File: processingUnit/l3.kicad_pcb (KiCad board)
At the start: 2 copper layers, 168.8 x 115 mm, 13 parts, among them J1 Conn_01x04, J2 Conn_01x06, J3 Conn_01x06, J4 Conn_01x06, J5 Conn_01x06, SW1 SW_SPDT, SW2 SW_SPDT, SW5 SW_SPDT, U2 BNO085, U3 >VALUE

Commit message: rough ideation
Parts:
- removed J1: Conn_01x04, Connector_JST:JST_XH_S4B-XH-A_1x04_P2.50mm_Horizontal
- removed J2, J3, J4, J5: Conn_01x06, Connector_JST:JST_SH_BM06B-SRSS-TB_1x06-1MP_P1.00mm_Vertical
- removed R1, R2: 1K, l3:res0603
- removed SW1, SW2, SW5: SW_SPDT, l3:SS12D00G3
- removed U1: ~, l3:OpenMV_RT
- removed U2: BNO085, l3:bno085
- removed U3: >VALUE, l3:xiao-esp32c3
- added C101: 2u2, Library:cap0603, F.Cu at (-13.5, 70.9)
- added C102: 2u2, Library:cap0603, F.Cu at (-13.5, 74.0)
- added C103: 2u2, Library:cap0603, F.Cu at (-13.5, 77.1)
- added C104: 2u2, Library:cap0603, F.Cu at (-13.5, 80.2)
- added C201: 100u, Capacitor_THT:CP_Radial_D8.0mm_P3.50mm, F.Cu at (-62.1, 74.1)
- added C202: 100u, Capacitor_THT:CP_Radial_D8.0mm_P3.50mm, F.Cu at (-62.1, 83.7)
- added C203: 0u1, Library:cap0603, F.Cu at (-43.7, 84.5)
- added C204: 0u1, Library:cap0603, F.Cu at (-43.7, 87.5)
- added C205: 100u, Capacitor_THT:CP_Radial_D8.0mm_P3.50mm, F.Cu at (-62.1, 93.2)
- added C206: 100u, Capacitor_THT:CP_Radial_D8.0mm_P3.50mm, F.Cu at (-62.1, 102.8)
- added C207: 0u1, Library:cap0603, F.Cu at (-43.7, 90.7)
- added C208: 0u1, Library:cap0603, F.Cu at (-43.7, 93.8)
- added C326: 2u2, Library:cap0603, F.Cu at (-63.0, 127.7)
- added C327: 0u1, Library:cap0603, F.Cu at (-63.0, 130.8)
- added C328: 0u1, Library:cap0603, F.Cu at (-63.0, 133.9)
- added C329: 0u1, Library:cap0603, F.Cu at (-63.0, 137.0)
- added C330: 0u1, Library:cap0603, F.Cu at (-58.3, 127.7)
- added C331: 0u1, Library:cap0603, F.Cu at (-58.3, 130.8)
- added C332: 0u1, Library:cap0603, F.Cu at (-58.3, 133.9)
- added C333: 2u2, Library:cap0603, F.Cu at (-58.3, 137.0)
- added C334: 0u1, Library:cap0603, F.Cu at (-53.6, 127.7)
- added C335: 10p, Library:cap0603, F.Cu at (-53.6, 130.8)
- added C336: 10p, Library:cap0603, F.Cu at (-53.6, 133.9)
- added C337: 10p, Library:cap0603, F.Cu at (-53.6, 137.0)
- added C338: 10p, Library:cap0603, F.Cu at (-48.9, 127.7)
- added C401: 2u2, Library:cap0603, F.Cu at (-34.8, 113.2)
- added C402: 0u1, Library:cap0603, F.Cu at (-34.8, 116.3)
- added C403: 0u1, Library:cap0603, F.Cu at (-34.8, 119.5)
- added C404: 0u1, Library:cap0603, F.Cu at (-34.8, 122.5)
- added C405: 0u1, Library:cap0603, F.Cu at (-34.8, 125.7)
- added C406: 0u1, Library:cap0603, F.Cu at (-34.8, 128.8)
- added C407: 0u1, Library:cap0603, F.Cu at (-34.8, 131.8)
- added C408: 10p, Library:cap0603, F.Cu at (-30.1, 113.2)
- added C409: 10p, Library:cap0603, F.Cu at (-30.1, 116.3)
- added C410: 0u1, Library:cap0603, F.Cu at (31.8, 138.8)
- added C411: 2u2, Library:cap0603, F.Cu at (31.8, 136.6)
- added C412: 10n, Library:cap0603, F.Cu at (34.7, 134.0)
- added C413: 0u1, Library:cap0603, F.Cu at (36.9, 134.0)
- added D304: RCLAMP0521PATCT, Library:RCLAMP0521PATCT, F.Cu at (-49.1, 120.0)
- added D305: RCLAMP0521PATCT, Library:RCLAMP0521PATCT, F.Cu at (-49.1, 122.8)
- added D306: RED, Library:led0603, F.Cu at (-48.9, 130.8)
- added D401: RCLAMP0521PATCT, Library:RCLAMP0521PATCT, F.Cu at (-14.2, 113.0)
- added D402: RCLAMP0521PATCT, Library:RCLAMP0521PATCT, F.Cu at (-14.2, 115.8)
- added D403: RED, Library:led0603, F.Cu at (43.6, 150.8)
- added FB101: 100R, Library:fb0603, F.Cu at (-13.5, 83.3)
- added FB102: 100R, Library:fb0603, F.Cu at (-13.5, 86.4)
- added IC201: TB67H450FNG,EL, Library:P-HSOP8-0405-1p27-001_TOS, F.Cu at (-50.6, 86.2)
- added IC202: TB67H450FNG,EL, Library:P-HSOP8-0405-1p27-001_TOS, F.Cu at (-50.6, 93.0)
- added IC203: TB67H450FNG,EL, Library:P-HSOP8-0405-1p27-001_TOS, F.Cu at (-50.6, 99.7)
- added IC204: TB67H450FNG,EL, Library:P-HSOP8-0405-1p27-001_TOS, F.Cu at (-50.6, 106.3)
- added IC401: ICM-42688-P, Library:IIM42352, F.Cu at (35.8, 137.7)
- added J101: +12V, Library:xt30-f, F.Cu at (101.4, 95.6)
- added J102: Conn_01x05, Connector_JST:JST_XH_B5B-XH-A_1x05_P2.50mm_Vertical, F.Cu at (108.4, 90.4)
- added J103: Conn_01x04, Connector_JST:JST_XH_B4B-XH-A_1x04_P2.50mm_Vertical, F.Cu at (181.0, 111.3)
- added J104: Conn_01x04, Connector_JST:JST_XH_B4B-XH-A_1x04_P2.50mm_Vertical, B.Cu at (187.8, 111.3)
- added J201: FL, Connector_JST:JST_XH_S2B-XH-A_1x02_P2.50mm_Horizontal, F.Cu at (-52.1, 72.7)
- added J202: FR, Connector_JST:JST_XH_S2B-XH-A_1x02_P2.50mm_Horizontal, F.Cu at (-42.7, 72.7)
- added J203: BL, Connector_JST:JST_XH_S2B-XH-A_1x02_P2.50mm_Horizontal, F.Cu at (-33.2, 72.7)
- added J204: BR, Connector_JST:JST_XH_S2B-XH-A_1x02_P2.50mm_Horizontal, F.Cu at (-23.8, 72.7)
- added J309: Conn_01x04, Connector_JST:JST_XH_B4B-XH-A_1x04_P2.50mm_Vertical, F.Cu at (187.8, 97.8)
- added J401: Conn_01x04, Connector_JST:JST_XH_B4B-XH-A_1x04_P2.50mm_Vertical, F.Cu at (181.0, 97.8)
- added Q401: NTR1P02T1G, Package_TO_SOT_SMD:SOT-23, F.Cu at (203.8, 100.2)
- added R201: 10K, Library:res0603, F.Cu at (-39.0, 84.5)
- added R202: 10K, Library:res0603, F.Cu at (-39.0, 87.5)
- added R203: 20, Library:res0603, F.Cu at (-39.0, 90.7)
- added R204: 20, Library:res0603, F.Cu at (-39.0, 93.8)
- added R205: 10K, Library:res0603, F.Cu at (-34.3, 84.5)
- added R206: 10K, Library:res0603, F.Cu at (-34.3, 87.5)
- added R207: 20, Library:res0603, F.Cu at (-34.3, 90.7)
- added R208: 20, Library:res0603, F.Cu at (-34.3, 93.8)
- added R313: 10K, Library:res0603, F.Cu at (-48.9, 133.9)
- added R314: 1K, Library:res0603, F.Cu at (-48.9, 137.0)
- added R401: R, Library:res0603, F.Cu at (-25.4, 113.2)
- added R402: R, Library:res0603, F.Cu at (40.4, 136.5)
- added R403: R, Library:res0603, F.Cu at (40.4, 139.6)
- added R404: 1K, Library:res0603, F.Cu at (43.7, 148.6)
- added R405: 10K, Library:res0603, F.Cu at (203.7, 104.0)
- added SW303: SW_Push, Library:SW_PUSH_SPST, F.Cu at (-43.9, 120.9)
- added SW401: SW_Push, Library:SW_PUSH_SPST, F.Cu at (-19.5, 113.9)
- added SW402: SW_Push, Library:SW_PUSH_SPST, F.Cu at (193.6, 100.8)
- added U303: STM32F446RET, Package_QFP:LQFP-64_10x10mm_P0.5mm, F.Cu at (-58.1, 118.9)
- added U304: 16MHz, Library:830108288709, F.Cu at (-44.2, 135.5)
- added U401: STM32F103CBTX, Package_QFP:LQFP-48_7x7mm_P0.5mm, F.Cu at (36.0, 146.7)
- added U402: 16MHz, Library:830108288709, F.Cu at (-20.7, 129.9)
- added Y301: 32.768 kHz, Library:830003000, F.Cu at (-45.0, 115.2)
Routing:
- removed copper zone on B.Cu, net GND
- removed copper zone on F.Cu, net GND
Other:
- board outline removed

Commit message: yes
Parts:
- removed C326, C333, C401, C411: 2u2, Library:cap0603
- removed C327, C328, C329, C330, C331, C332, C334, C402, C403, C404, C405, C406, C407, C410, C413: 0u1, Library:cap0603
- removed C335, C336, C337, C338, C408, C409: 10p, Library:cap0603
- removed C412: 10n, Library:cap0603
- removed D304, D305, D401, D402: RCLAMP0521PATCT, Library:RCLAMP0521PATCT
- removed D306, D403: RED, Library:led0603
- removed IC202, IC203, IC204: TB67H450FNG,EL, Library:P-HSOP8-0405-1p27-001_TOS
- removed IC401: ICM-42688-P, Library:IIM42352
- removed J202: FR, Connector_JST:JST_XH_S2B-XH-A_1x02_P2.50mm_Horizontal
- removed J203: BL, Connector_JST:JST_XH_S2B-XH-A_1x02_P2.50mm_Horizontal
- removed J204: BR, Connector_JST:JST_XH_S2B-XH-A_1x02_P2.50mm_Horizontal
- removed J309, J401: Conn_01x04, Connector_JST:JST_XH_B4B-XH-A_1x04_P2.50mm_Vertical
- removed Q401: NTR1P02T1G, Package_TO_SOT_SMD:SOT-23
- removed R206, R313, R405: 10K, Library:res0603
- removed R207, R208: 20, Library:res0603
- removed R314, R404: 1K, Library:res0603
- removed R401, R402, R403: R, Library:res0603
- removed SW303, SW401, SW402: SW_Push, Library:SW_PUSH_SPST
- removed U303: STM32F446RET, Package_QFP:LQFP-64_10x10mm_P0.5mm
- removed U304, U402: 16MHz, Library:830108288709
- removed U401: STM32F103CBTX, Package_QFP:LQFP-48_7x7mm_P0.5mm
- added C209: 10n, Library:cap0603, F.Cu at (39.7, 82.5)
- added C210: 0u1, Library:cap0603, F.Cu at (39.7, 85.6)
- added C211: 0u1, Library:cap0603, F.Cu at (39.7, 88.7)
- added C212: 10p, Library:cap0603, F.Cu at (39.7, 91.8)
- added C213: 10p, Library:cap0603, F.Cu at (39.7, 94.9)
- added C301: 0u1, Library:cap0603, F.Cu at (35.0, 42.4)
- added C302: 10p, Library:cap0603, F.Cu at (35.0, 45.5)
- added C303: 10p, Library:cap0603, F.Cu at (35.0, 48.6)
- added C304: 10p, Library:cap0603, F.Cu at (35.0, 51.7)
- added C305: 10p, Library:cap0603, F.Cu at (39.7, 42.4)
- added C306: 2u2, Library:cap0603, F.Cu at (39.7, 45.5)
- added C307: 2u2, Library:cap0603, F.Cu at (39.7, 48.6)
- added C308: 0u1, Library:cap0603, F.Cu at (39.7, 51.7)
- added C309: 0u1, Library:cap0603, F.Cu at (44.4, 42.4)
- added C310: 0u1, Library:cap0603, F.Cu at (44.4, 45.5)
- added C311: 0u1, Library:cap0603, F.Cu at (44.4, 48.6)
- added C312: 0u1, Library:cap0603, F.Cu at (44.4, 51.7)
- added C313: 0u1, Library:cap0603, F.Cu at (49.1, 42.4)
- added D201: RCLAMP0521PATCT, Library:RCLAMP0521PATCT, F.Cu at (55.6, 94.8)
- added D202: RCLAMP0521PATCT, Library:RCLAMP0521PATCT, F.Cu at (55.6, 97.5)
- added D203: RED, Library:led0603, F.Cu at (39.7, 98.0)
- added D301: RED, Library:led0603, F.Cu at (49.1, 45.5)
- added D302: RCLAMP0521PATCT, Library:RCLAMP0521PATCT, F.Cu at (53.2, 46.7)
- added D303: RCLAMP0521PATCT, Library:RCLAMP0521PATCT, F.Cu at (53.2, 49.4)
- added J301: Conn_01x04, Connector_JST:JST_XH_B4B-XH-A_1x04_P2.50mm_Vertical, F.Cu at (36.1, 56.6)
- added Q201: NTR1P02T1G, Package_TO_SOT_SMD:SOT-23, F.Cu at (49.6, 72.5)
- added R301: 1K, Library:res0603, F.Cu at (49.1, 48.6)
- added R302: 10K, Library:res0603, F.Cu at (49.1, 51.7)
- added SW201: SW_Push, Library:SW_PUSH_SPST, F.Cu at (50.3, 91.5)
- added SW202: SW_Push, Library:SW_PUSH_SPST, F.Cu at (50.3, 95.9)
- added SW301: SW_Push, Library:SW_PUSH_SPST, F.Cu at (55.0, 43.1)
- added U201: STM32F103CBTX, Package_QFP:LQFP-48_7x7mm_P0.5mm, F.Cu at (52.5, 83.5)
- added U202: 16MHz, Library:830108288709, F.Cu at (56.1, 91.3)
- added U301: STM32F446RET, Package_QFP:LQFP-64_10x10mm_P0.5mm, F.Cu at (54.4, 60.5)
- added U302: 16MHz, Library:830108288709, F.Cu at (57.3, 47.5)
- C201: value 100u -> 2u2; footprint Capacitor_THT:CP_Radial_D8.0mm_P3.50mm -> Library:cap0603
- C202, C205, C206: value 100u -> 0u1; footprint Capacitor_THT:CP_Radial_D8.0mm_P3.50mm -> Library:cap0603
- C208: value 0u1 -> 2u2
- IC201: value TB67H450FNG,EL -> ICM-42688-P; footprint Library:P-HSOP8-0405-1p27-001_TOS -> Library:IIM42352
- J104: moved to F.Cu
- J201: value FL -> Conn_01x04; footprint Connector_JST:JST_XH_S2B-XH-A_1x02_P2.50mm_Horizontal -> Connector_JST:JST_XH_B4B-XH-A_1x04_P2.50mm_Vertical
- R202: value 10K -> R
- R203, R204: value 20 -> R
- R205: value 10K -> 1K
- moved J104 125.8 mm to (64.0, 89.0), turned to 0 degrees
- moved J103 120.8 mm to (64.0, 81.2), turned to 0 degrees
- moved IC201 105.9 mm to (54.4, 72.2)
- moved Y301 97.7 mm to (38.6, 64.6)
- moved C206 97.5 mm to (35.0, 94.9)
- moved C201 97.3 mm to (35.0, 79.4)
- moved C205 97.2 mm to (35.0, 91.8)
- moved C202 97.2 mm to (35.0, 82.5)
- moved C101 91.1 mm to (77.3, 79.4)
- moved C102 91.1 mm to (77.3, 82.5)
- moved C103 91.1 mm to (77.3, 85.6)
- moved C104 91.1 mm to (77.3, 88.7)
- moved FB101 91.1 mm to (77.3, 91.8)
- moved FB102 91.1 mm to (77.3, 94.9)
- moved J201 88.3 mm to (36.1, 73.5)
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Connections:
- C201 pad 1: +12V -> +3V3 FILT
- C202 pad 1: +12V -> +3V3 FILT
- C203 pad 1: /Motor Driver/FL VREF -> +3V3 FILT
- C204 pad 1: /Motor Driver/FR VREF -> +3V3 FILT
- C205 pad 1: +12V -> +3V3 FILT
- C206 pad 1: +12V -> +3V3 FILT
- C207 pad 1: /Motor Driver/BL VREF -> Net-(IC201-VDD)
- C208 pad 1: /Motor Driver/BR VREF -> Net-(IC201-VDD)
- IC201 pad 1: GNDREF -> unconnected-(IC201-SDO-Pad1)
- IC201 pad 2: FL IN 2 -> GNDREF
- IC201 pad 3: FL IN 1 -> GNDREF
- IC201 pad 4: /Motor Driver/FL VREF -> unconnected-(IC201-INT1-Pad4)
- IC201 pad 5: +12V -> Net-(IC201-VDD)
- IC201 pad 6: /Motor Driver/FL OUT 1 -> GNDREF
- IC201 pad 7: Net-(IC201-RS) -> GNDREF
- IC201 pad 8: /Motor Driver/FL OUT 2 -> Net-(IC201-VDD)
- IC201 pad 9: GNDREF -> unconnected-(IC201-INT2-Pad9)
- J201 pad 1: /Motor Driver/FL OUT 1 -> +3V3
- J201 pad 2: /Motor Driver/FL OUT 2 -> /IMU/MCU SWDIO
- R201 pad 1: +5V FILT -> Net-(Q201-G)
- R201 pad 2: /Motor Driver/FL VREF -> GNDREF
- R202 pad 1: +5V FILT -> GNDREF
- R202 pad 2: /Motor Driver/FR VREF -> /IMU/MCU BOOT0
- R203 pad 1: Net-(IC201-RS) -> +3V3 FILT
- R203 pad 2: GNDREF -> /IMU/MPU SDA
- R204 pad 1: Net-(IC202-RS) -> +3V3 FILT
- R204 pad 2: GNDREF -> /IMU/MPU SCL
- R205 pad 1: +5V FILT -> Net-(D203-K)
- R205 pad 2: /Motor Driver/BL VREF -> GNDREF

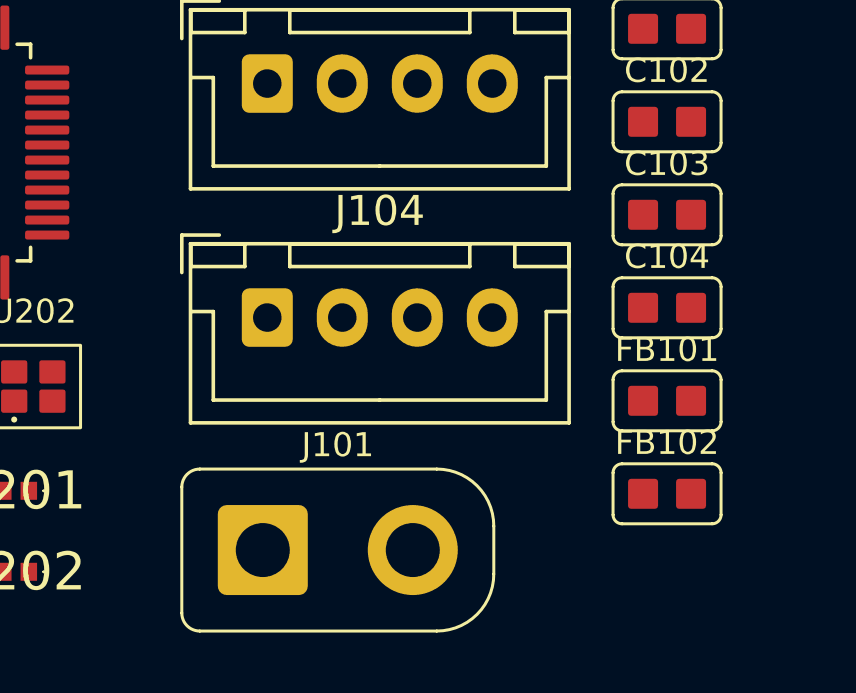
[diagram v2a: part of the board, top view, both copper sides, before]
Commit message: modified motor driver removed topInterface
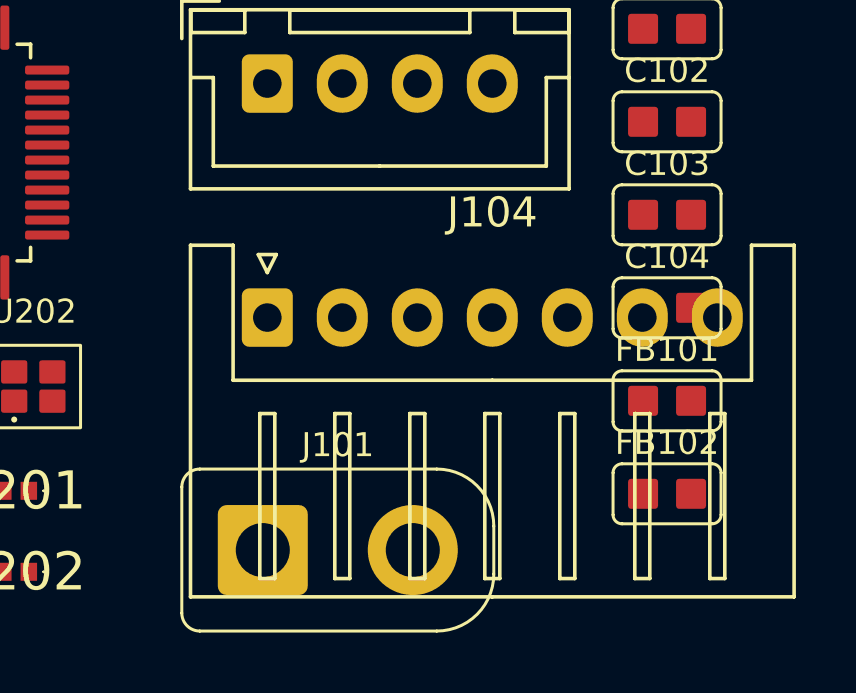
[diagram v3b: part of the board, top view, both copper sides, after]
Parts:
- J104: value Conn_01x04 -> Conn_01x07; footprint Connector_JST:JST_XH_B4B-XH-A_1x04_P2.50mm_Vertical -> Connector_JST:JST_XH_S7B-XH-A_1x07_P2.50mm_Horizontal
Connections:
- J104 pad 1: +5V -> +3V3
- J104 pad 4: GNDREF -> unconnected-(J104-Pin_4-Pad4)

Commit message: 死
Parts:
- removed C208: 2u2, Library:cap0603
- removed C209: 10n, Library:cap0603
- removed C210, C211, C311, C312, C313: 0u1, Library:cap0603
- removed C212, C213: 10p, Library:cap0603
- removed D202, D302, D303: RCLAMP0521PATCT, Library:RCLAMP0521PATCT
- removed D203: RED, Library:led0603
- removed IC201: ICM-42688-P, Library:IIM42352
- removed J104: Conn_01x07, Connector_JST:JST_XH_S7B-XH-A_1x07_P2.50mm_Horizontal
- removed J201, J301: Conn_01x04, Connector_JST:JST_XH_B4B-XH-A_1x04_P2.50mm_Vertical
- removed Q201: NTR1P02T1G, Package_TO_SOT_SMD:SOT-23
- removed R203, R204: R, Library:res0603
- removed R205: 1K, Library:res0603
- removed SW202: SW_Push, Library:SW_PUSH_SPST
- removed U202: 16MHz, Library:830108288709
- added R303: 4K7, Library:res0603, F.Cu at (61.5, 24.7)
- added R304: 4K7, Library:res0603, F.Cu at (61.5, 27.8)
- added R305: 1K, Library:res0603, F.Cu at (61.5, 30.9)
- added SW302: IMU RST, Button_Switch_THT:SW_PUSH_6mm, F.Cu at (47.0, 43.0)
- added Y201: 8Mhz, Crystal:Resonator_SMD_Murata_CSTxExxV-3Pin_3.0x1.1mm, F.Cu at (47.6, 68.8)
- C207, C309, C310: value 0u1 -> C
- C301: value 0u1 -> 2u2
- C302, C304, C305: value 10p -> 0u1
- C303: value 10p -> 2u2
- C306, C307: value 2u2 -> 0u1
- D201: value RCLAMP0521PATCT -> RED; footprint Library:RCLAMP0521PATCT -> Library:led0603
- J101: value +12V -> Conn_01x05; footprint Library:xt30-f -> Connector_JST:JST_XH_B5B-XH-A_1x05_P2.50mm_Vertical
- J102: value Conn_01x05 -> Conn_01x04; footprint Connector_JST:JST_XH_B5B-XH-A_1x05_P2.50mm_Vertical -> Connector_JST:JST_XH_B4B-XH-A_1x04_P2.50mm_Vertical
- J103: value Conn_01x04 -> Conn_01x07; footprint Connector_JST:JST_XH_B4B-XH-A_1x04_P2.50mm_Vertical -> Connector_JST:JST_XH_S7B-XH-A_1x07_P2.50mm_Horizontal
- R201, R302: value 10K -> R
- R202: value R -> 1K
- R301: value 1K -> 10K
- SW201: value SW_Push -> ENC RST; footprint Library:SW_PUSH_SPST -> Button_Switch_THT:SW_PUSH_6mm
- SW301: value SW_Push -> IMU RST; footprint Library:SW_PUSH_SPST -> Button_Switch_THT:SW_PUSH_6mm
- U201: value STM32F103CBTX -> STM32F103Cx; footprint Package_QFP:LQFP-48_7x7mm_P0.5mm -> Package_DFN_QFN:QFN-48-1EP_7x7mm_P0.5mm_EP5.6x5.6mm_ThermalVias
- U301: value STM32F446RET -> STM32F103Cx; footprint Package_QFP:LQFP-64_10x10mm_P0.5mm -> Package_DFN_QFN:QFN-48-1EP_7x7mm_P0.5mm_EP5.6x5.6mm_ThermalVias
- U302: value 16MHz -> BNO085; footprint Library:830108288709 -> Library:bno085
- Y301: value 32.768 kHz -> 8Mhz; footprint Library:830003000 -> Crystal:Resonator_SMD_Murata_CSTxExxV-3Pin_3.0x1.1mm
- moved J101 70.4 mm to (29.2, 37.0)
- moved J103 70.0 mm to (24.5, 23.4)
- moved C102 69.7 mm to (23.4, 38.2)
- moved C101 69.7 mm to (23.4, 35.1)
- moved C103 69.7 mm to (23.4, 41.3)
- moved C104 69.7 mm to (23.4, 44.4)
- moved FB101 69.7 mm to (23.4, 47.5)
- moved FB102 69.7 mm to (23.4, 50.6)
- moved C206 45.2 mm to (52.1, 53.1)
- moved C207 45.2 mm to (52.1, 56.2)
- moved J102 45.0 mm to (29.2, 44.8)
- moved SW201 38.4 mm to (56.4, 53.6)
- moved D201 35.7 mm to (52.1, 59.3)
- moved R302 32.6 mm to (61.5, 21.6)
- moved C202 29.1 mm to (47.4, 56.2)
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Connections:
- net BL IN 1 renamed /IMU/IMU SWCLK
- net BR IN 1 renamed /IMU/TNSY MISO
- net BR IN 2 renamed /IMU/TNSY MOSI
- C207 pad 1: Net-(IC201-VDD) -> /ENC/ENC RST
- C301 pad 1: /STM32F4/MCU RST -> +3V3 FILT
- C302 pad 1: /STM32F4/MCU OSC OUT -> +3V3 FILT
- C303 pad 1: /STM32F4/MCU OSC IN -> +3V3 FILT
- C304 pad 1: /STM32F4/MCU OSC 32 OUT -> +3V3 FILT
- C305 pad 1: /STM32F4/MCU OSC 32 IN -> +3V3 FILT
- C306 pad 1: /STM32F4/VCAP -> +3V3 FILT
- C309 pad 1: +3V3 FILT -> /IMU/BNO RST
- C310 pad 1: +3V3 FILT -> /IMU/IMU RST
- D201 pad 1: GNDREF -> Net-(D201-K)
- D201 pad 2: /IMU/MCU SWDIO -> /ENC/ENC LED
- D301 pad 2: /STM32F4/MCU LED -> /IMU/IMU LED
- J101 pad 1: +12V -> +5V
- J101 pad 2: GNDREF -> +3V3
- J102 pad 2: +3V3 -> CAM RX
- J102 pad 3: KICK SIG -> CAM TX
- J103 pad 1: +5V -> +3V3
- J103 pad 2: CAM RX -> LIGHT RX
- J103 pad 3: CAM TX -> LIGHT TX
- J103 pad 4: GNDREF -> unconnected-(J103-Pin_4-Pad4)
- R201 pad 1: Net-(Q201-G) -> GNDREF
- R201 pad 2: GNDREF -> /ENC/ENC BOOT0
- R202 pad 1: GNDREF -> Net-(D201-K)
- R202 pad 2: /IMU/MCU BOOT0 -> GNDREF
- R301 pad 1: Net-(D301-K) -> +3V3 FILT
- R301 pad 2: GNDREF -> /IMU/BNO RST
- R302 pad 1: /STM32F4/MCU BOOT0 -> GNDREF
- R302 pad 2: GNDREF -> /IMU/IMU BOOT0
- SW201 pad 1: Net-(Q201-G) -> GNDREF
- SW201 pad 2: +3V3 FILT -> /ENC/ENC RST
- SW301 pad 2: /STM32F4/MCU RST -> /IMU/BNO RST
- U201 pad 10: unconnected-(U201C-PA0-Pad10) -> /ENC/M1 ENC A
- U201 pad 11: unconnected-(U201C-PA1-Pad11) -> /ENC/M1 ENC B
- U201 pad 12: unconnected-(U201C-PA2-Pad12) -> /ENC/M1 IN A
- U201 pad 13: unconnected-(U201C-PA3-Pad13) -> /ENC/M1 IN B
- U201 pad 14: unconnected-(U201C-PA4-Pad14) -> /ENC/ENC NSS
- U201 pad 15: unconnected-(U201C-PA5-Pad15) -> /ENC/TNSY SCK
- U201 pad 16: unconnected-(U201C-PA6-Pad16) -> /ENC/TNSY MISO
- U201 pad 17: unconnected-(U201C-PA7-Pad17) -> /ENC/TNSY MOSI
- U201 pad 21: unconnected-(U201C-PB10-Pad21) -> /ENC/M2 IN B
- U201 pad 22: unconnected-(U201C-PB11-Pad22) -> /ENC/M3 IN A
- U201 pad 26: unconnected-(U201C-PB13-Pad26) -> /ENC/M3 IN B
- U201 pad 27: unconnected-(U201C-PB14-Pad27) -> /ENC/M4 IN A
- U201 pad 28: /IMU/MCU1 LED -> unconnected-(U201C-PB15-Pad28)
- U201 pad 29: unconnected-(U201C-PA8-Pad29) -> /ENC/M3 ENC A
- U201 pad 30: IMU TX -> /ENC/M3 ENC B
- U201 pad 31: IMU RX -> /ENC/M2 IN A
- U201 pad 34: /IMU/MCU SWDIO -> /ENC/ENC SWDIO
- U201 pad 37: /IMU/MCU SWCLK -> /ENC/ENC SWCLK
- U201 pad 38: unconnected-(U201C-PA15-Pad38) -> /ENC/ENC LED
- U201 pad 40: unconnected-(U201C-PB4-Pad40) -> /ENC/M4 ENC A
- U201 pad 41: unconnected-(U201C-PB5-Pad41) -> /ENC/M4 ENC B
- U201 pad 42: /IMU/MPU SCL -> /ENC/M2 ENC A
- U201 pad 43: /IMU/MPU SDA -> /ENC/M2 ENC B
- U201 pad 44: /IMU/MCU BOOT0 -> /ENC/ENC BOOT0
- U201 pad 5: /IMU/MCU1 OSC IN -> /ENC/ENC OSC IN
- U201 pad 6: /IMU/MCU1 OSC OUT -> /ENC/ENC OSC OUT
- U201 pad 7: /IMU/MCU RST -> /ENC/ENC RST
- U301 pad 12: GNDREF -> unconnected-(U301C-PA2-Pad12)
- U301 pad 13: +3V3 FILT -> unconnected-(U301C-PA3-Pad13)
- U301 pad 14: CAM TX -> /IMU/IMU NSS
- U301 pad 15: CAM RX -> /IMU/TNSY SCK
- U301 pad 18: GNDREF -> unconnected-(U301C-PB0-Pad18)
- U301 pad 19: +3V3 FILT -> unconnected-(U301C-PB1-Pad19)
- U301 pad 2: /STM32F4/MCU LED -> unconnected-(U301B-PC13-Pad2)
- U301 pad 21: FR IN 1 -> unconnected-(U301C-PB10-Pad21)
- U301 pad 22: FR IN 2 -> unconnected-(U301C-PB11-Pad22)
- U301 pad 23: D1 IN 1 -> GNDREF
- U301 pad 24: unconnected-(U301B-PC4-Pad24) -> +3V3 FILT
- U301 pad 28: KICK SIG -> unconnected-(U301C-PB15-Pad28)
- U301 pad 3: /STM32F4/MCU OSC 32 IN -> unconnected-(U301B-PC14-Pad3)
- U301 pad 30: /STM32F4/VCAP -> unconnected-(U301C-PA9-Pad30)
- U301 pad 31: GNDREF -> unconnected-(U301C-PA10-Pad31)
- U301 pad 32: +3V3 FILT -> unconnected-(U301C-PA11-Pad32)
- U301 pad 34: unconnected-(U301B-PB13-Pad34) -> /IMU/IMU SWDIO
- U301 pad 35: unconnected-(U301B-PB14-Pad35) -> GNDREF
- U301 pad 36: unconnected-(U301B-PB15-Pad36) -> +3V3 FILT
- U301 pad 38: BL IN 2 -> /IMU/IMU LED
- U301 pad 39: FL IN 1 -> unconnected-(U301C-PB3-Pad39)
- U301 pad 4: /STM32F4/MCU OSC 32 OUT -> unconnected-(U301B-PC15-Pad4)
- U301 pad 40: FL IN 2 -> unconnected-(U301C-PB4-Pad40)
- U301 pad 41: D1 IN 2 -> unconnected-(U301C-PB5-Pad41)
- U301 pad 42: LIGHT TX -> /IMU/IMU SCL
- U301 pad 43: LIGHT RX -> /IMU/IMU SDA
- U301 pad 44: unconnected-(U301B-PA11-Pad44) -> /IMU/IMU BOOT0
- U301 pad 46: /STM32F4/MCU SWDIO -> unconnected-(U301C-PB9-Pad46)
- U301 pad 49: /STM32F4/MCU SWCLK -> GNDREF
- U301 pad 5: /STM32F4/MCU OSC IN -> /IMU/IMU OSC IN
- U301 pad 6: /STM32F4/MCU OSC OUT -> /IMU/IMU OSC OUT
- U301 pad 7: /STM32F4/MCU RST -> /IMU/IMU RST
- U301 pad 8: unconnected-(U301B-PC0-Pad8) -> GNDREF
- U301 pad 9: unconnected-(U301B-PC1-Pad9) -> +3V3 FILT
- Y301 pad 1: /STM32F4/MCU OSC 32 OUT -> /IMU/IMU OSC IN
- Y301 pad 2: unconnected-(Y301-Pad2) -> /IMU/IMU OSC OUT
- Y301 pad 3: unconnected-(Y301-Pad3) -> GNDREF
